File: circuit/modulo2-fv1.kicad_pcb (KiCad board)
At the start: 2 copper layers, 105 x 47 mm, 66 parts, among them J1 CONN_01X04, J2 POWER, J3 CONN_01X02, J4 HOLE, J5 HOLE, J6 USB_OTG, SW1 ROTENC_BOURNS_PEL12D, U1 NE5532, U10 TLE2426, U3 FV-1, U4 AVR-ISP6, U5 LM1117 3V3, U6 ATmega328p, U7 DBG_UART, U8 74164, Y1 16MHz

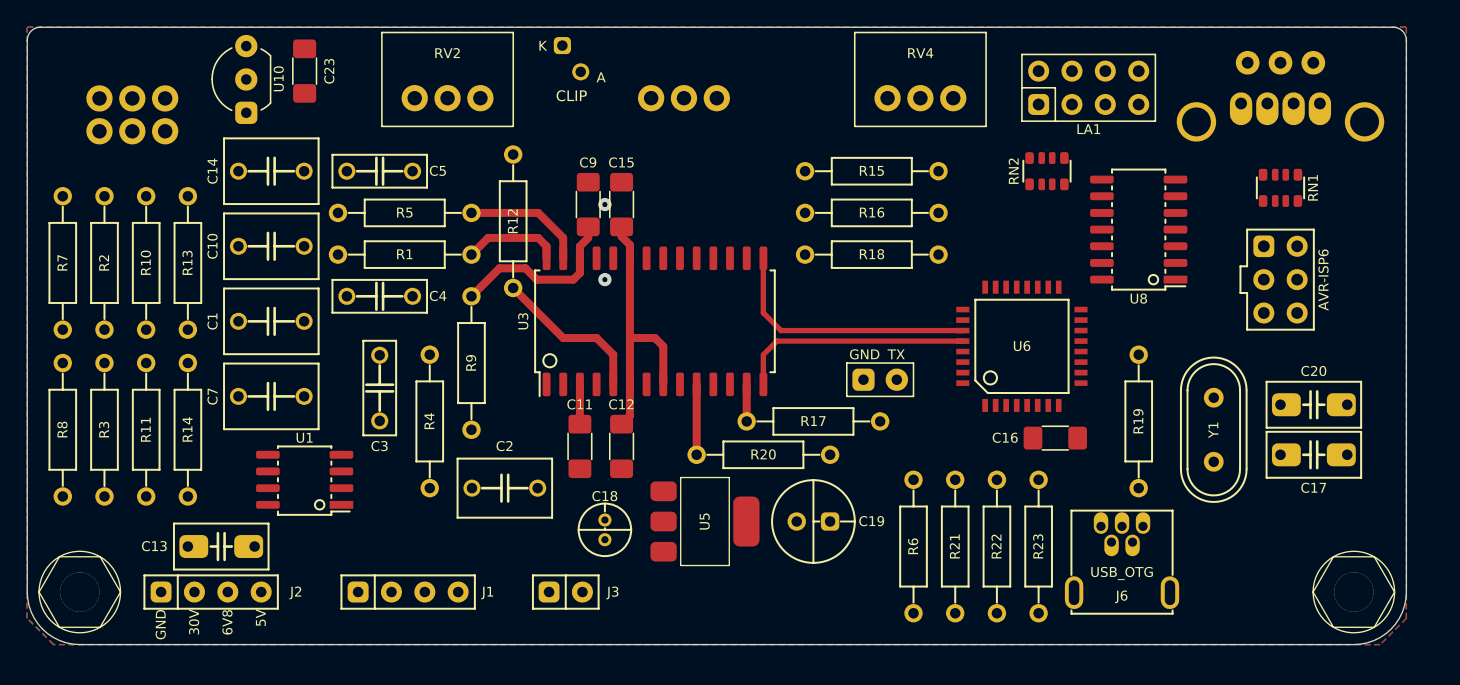
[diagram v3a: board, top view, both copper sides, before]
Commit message: routed pa27; routing fv-1
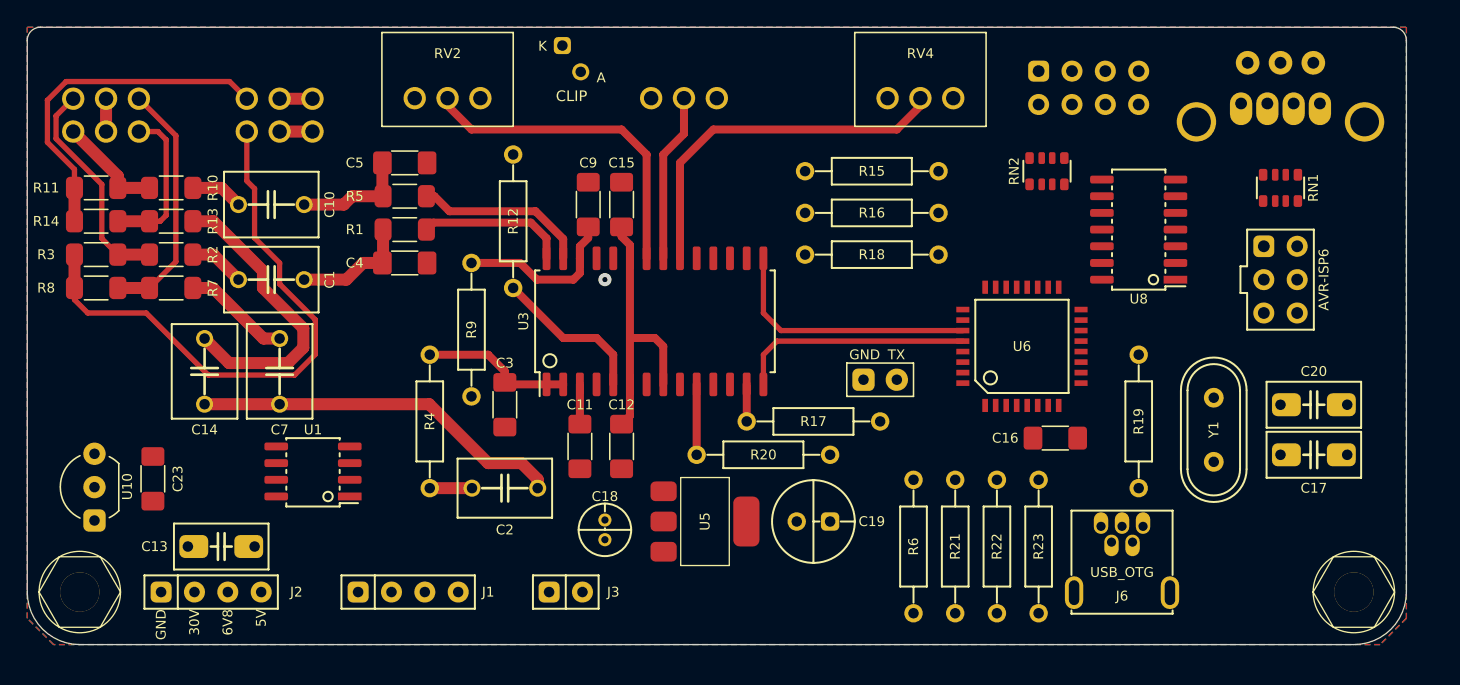
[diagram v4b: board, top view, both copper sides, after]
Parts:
- added RV5: A50K, myAmp:BOURNS_PTD902_xx15K, B.Cu at (69.2, 57.9)
- C3, C4, C5: footprint myAmp:C_FILM_L7.2mm_W2.5mm_P5.00mm -> myAmp:C_1206
- LA1: moved to B.Cu
- R1, R10, R11, R13, R14, R2, R3, R5, R7, R8: footprint myAmp:R_10MM -> myAmp:R_1206
- R23: value 1K5 -> 1M
- moved U10 33.1 mm to (55.1, 85.0)
- moved C23 33.1 mm to (59.6, 84.4)
- moved R11 18.8 mm to (55.2, 62.2), turned to 180 degrees
- moved R14 17.3 mm to (55.2, 64.8), turned to 180 degrees
- moved C14 16.1 mm to (63.5, 76.2), turned to 90 degrees
- moved R3 13.4 mm to (55.2, 67.3), turned to 180 degrees
- moved R8 11.1 mm to (55.2, 69.8), turned to 180 degrees
- moved C3 9.61 mm to (86.4, 78.7)
- moved R7 8.47 mm to (61.0, 69.8), turned to 180 degrees
- moved R10 6.02 mm to (61.0, 62.2), turned to 180 degrees
- moved R2 5.12 mm to (61.0, 67.3), turned to 180 degrees
- moved R13 3.42 mm to (61.0, 64.8), turned to 180 degrees
- moved C4 3.18 mm to (78.7, 67.9)
- moved C1 3.17 mm to (68.6, 69.2)
- moved C10 3.17 mm to (68.6, 63.5)
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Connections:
- R11 pad 2: Net-(R11-Pad2) -> Net-(RV5-Pad4)
- R14 pad 2: Net-(R11-Pad2) -> Net-(RV5-Pad4)
- R3 pad 2: Net-(R3-Pad2) -> Net-(RV5-Pad1)
- R8 pad 2: Net-(R3-Pad2) -> Net-(RV5-Pad1)
- RV1 pad 1: Net-(R2-Pad2) -> Net-(R10-Pad2)
- RV1 pad 3: Net-(R7-Pad2) -> Net-(R13-Pad2)
- RV1 pad 4: Net-(R10-Pad2) -> Net-(R2-Pad2)
- RV1 pad 6: Net-(R13-Pad2) -> Net-(R7-Pad2)
- U1 pad 2: /OUTL -> Net-(RV5-Pad1)
- U1 pad 3: Net-(R3-Pad2) -> VGND
- U1 pad 5: Net-(R11-Pad2) -> VGND
- U1 pad 6: /OUTR -> Net-(RV5-Pad4)
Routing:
- net Net-(RV5-Pad1): track 0.00 -> 43.9 mm
- net IN: track 0.00 -> 28.4 mm
- net Net-(RV4-Pad2): track 0.00 -> 28.0 mm
- net Net-(RV5-Pad4): track 0.00 -> 26.4 mm
- net Net-(RV2-Pad2): track 0.00 -> 25.2 mm
- net Net-(C14-Pad2): track 0.00 -> 22.8 mm
- net Net-(R7-Pad2): track 0.00 -> 18.8 mm
- net Net-(R2-Pad2): track 0.00 -> 16.8 mm
- net Net-(RV3-Pad2): track 0.00 -> 12.8 mm
- net Net-(R13-Pad2): track 0.00 -> 12.0 mm
- net Net-(C3-Pad2): track 0.00 -> 11.6 mm
- net /FVL: track 0.00 -> 9.05 mm
- net /FVR: track 0.00 -> 8.83 mm
- net Net-(C7-Pad2): track 0.00 -> 8.20 mm
- net Net-(R10-Pad2): track 0.00 -> 8.11 mm
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
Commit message: further routing of FV-1
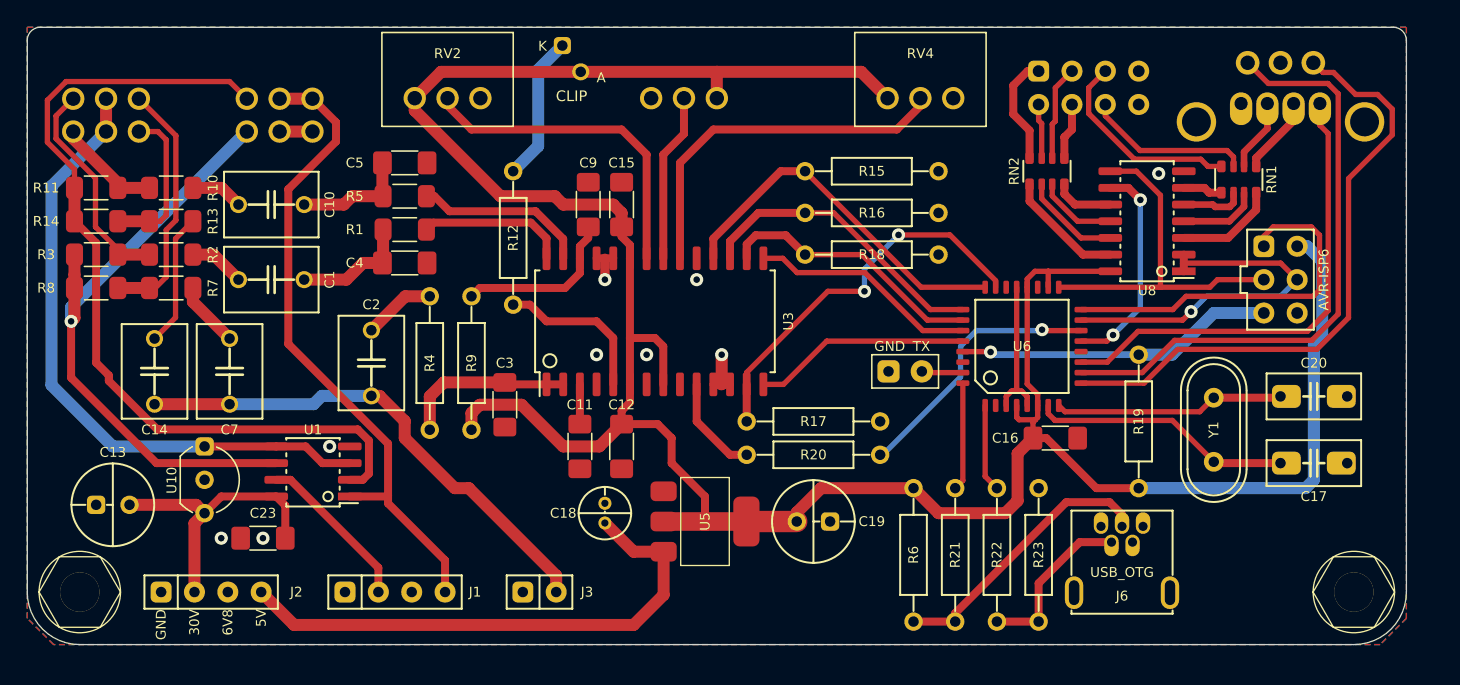
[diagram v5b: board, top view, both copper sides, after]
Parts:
- C13: value 100nF -> 10uF; footprint myAmp:C_5MM_1206 -> myAmp:CPOL_D6.3_P2.5
- C2: footprint myAmp:C_FILM_L7.2mm_W4.5mm_P5.00mm -> myAmp:C_FILM_L7.2mm_W5.0mm_P5.00mm
- moved C2 13.9 mm to (76.2, 75.6), turned to -90 degrees
- moved C23 9.52 mm to (67.9, 88.9), turned to 0 degrees
- moved C13 8.84 mm to (56.5, 86.4)
- moved U10 8.40 mm to (63.5, 84.5), turned to -90 degrees
- moved R4 4.45 mm to (80.6, 75.6), turned to -90 degrees
- moved C14 3.81 mm to (59.7, 76.2)
- moved C7 3.81 mm to (65.4, 76.2)
- moved R20 3.81 mm to (109.9, 82.5)
- moved RN1 3.24 mm to (142.2, 61.6)
- moved R9 2.54 mm to (83.8, 75.6)
- moved U7 2.01 mm to (116.8, 76.2)
- moved J3 2.00 mm to (89.0, 93.0)
- moved R12 1.27 mm to (87.0, 66.0)
- moved C18 1.27 mm to (94.0, 87.0)
- moved J1 1.00 mm to (78.0, 93.0)
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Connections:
- C13 pad 1: GND -> +24V
- C13 pad 2: +24V -> GND
- R11 pad 2: Net-(RV5-Pad4) -> Net-(R11-Pad2)
- R14 pad 2: Net-(RV5-Pad4) -> Net-(R11-Pad2)
- R3 pad 2: Net-(RV5-Pad1) -> Net-(R3-Pad2)
- R8 pad 2: Net-(RV5-Pad1) -> Net-(R3-Pad2)
- RV5 pad 1: Net-(RV5-Pad1) -> Net-(R3-Pad2)
- RV5 pad 4: Net-(RV5-Pad4) -> Net-(R11-Pad2)
- U1 pad 1: /OUTL -> /OUTR
- U1 pad 2: Net-(RV5-Pad1) -> Net-(R11-Pad2)
- U1 pad 6: Net-(RV5-Pad4) -> Net-(R3-Pad2)
- U1 pad 7: /OUTR -> /OUTL
- U6 pad 13: unconnected-(U6-Pad13) -> /LED_RST
- U6 pad 23: /LED_RST -> /T0
- U6 pad 30: /T0 -> unconnected-(U6-Pad30)
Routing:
- net +3V3: track 21.2 -> 208.7 mm
- net Net-(R11-Pad2): track 0.00 -> 65.5 mm
- net Net-(R3-Pad2): track 0.00 -> 47.8 mm, vias 0 -> 1
- net /OUTR: track 2.50 -> 50.2 mm
- net /ROT_B: track 0.00 -> 47.2 mm
- net VGND: track 2.50 -> 48.7 mm
- net /ROT_A: track 0.00 -> 46.1 mm
- net Net-(RV5-Pad1): track 43.9 -> 0.00 mm
- net +5V: track 0.00 -> 41.3 mm
- net /ROT_SW: track 0.00 -> 36.5 mm
- net /MISO: track 0.00 -> 28.5 mm
- net /MOSI: track 0.00 -> 28.2 mm, vias 0 -> 1
- net /S2: track 0.00 -> 28.0 mm
- net /SCK: track 0.00 -> 27.4 mm
- net /T0: track 2.82 -> 30.0 mm, vias 0 -> 2
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
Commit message: no more assembler; more routing
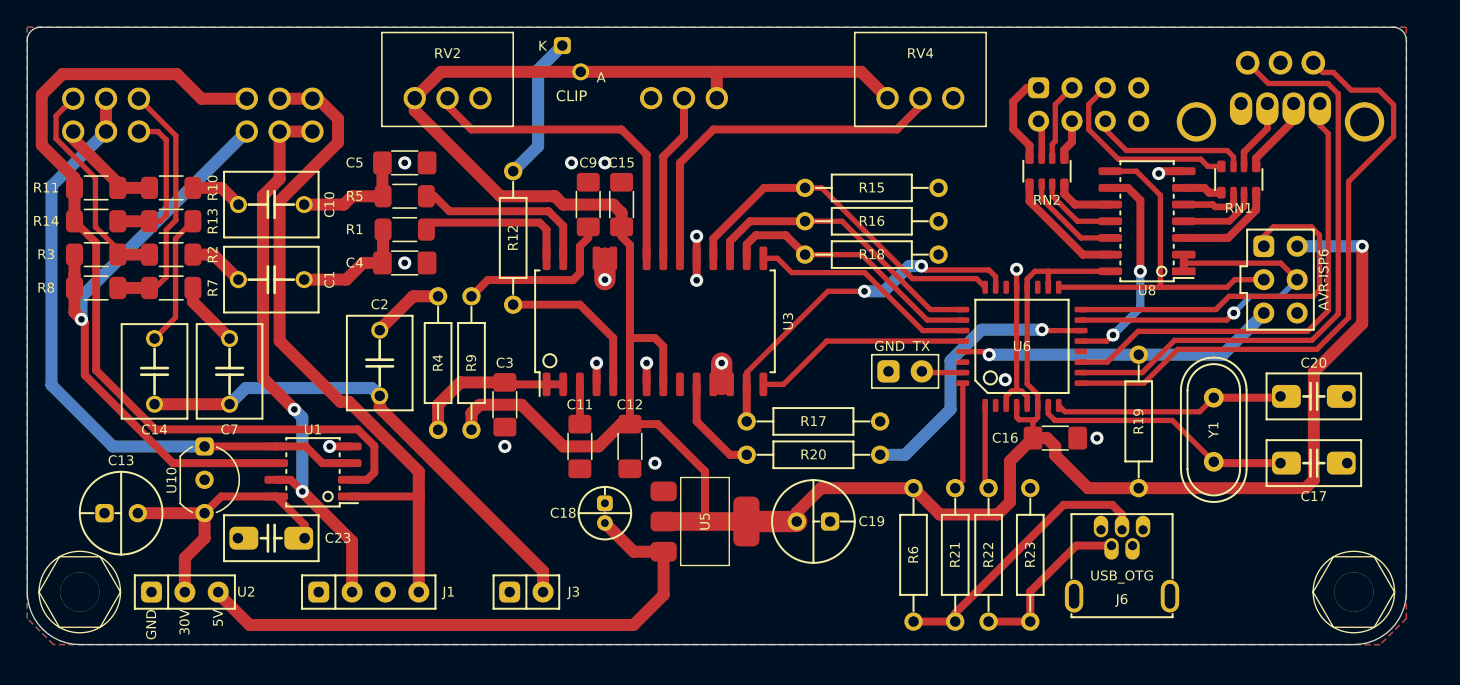
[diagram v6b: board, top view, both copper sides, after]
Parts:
- removed J2: POWER, myAmp:POWER
- added U2: POWER, myAmp:PWR_CONN, F.Cu at (62.0, 93.0)
- C23: footprint myAmp:C_1206 -> myAmp:C_5MM_1206
- moved J1 2.00 mm to (76.0, 93.0)
- moved LA1 1.27 mm to (130.8, 55.9)
- moved R15 1.27 mm to (114.3, 62.2)
- moved J3 1.00 mm to (88.0, 93.0)
- moved C13 0.90 mm to (57.1, 87.0)
- moved C12 0.64 mm to (95.9, 81.9)
- moved C23 0.64 mm to (68.6, 88.9)
- moved R22 0.64 mm to (123.2, 90.2)
- moved R23 0.64 mm to (126.4, 90.2)
- moved R4 0.64 mm to (81.3, 75.6)
- moved C2 0.63 mm to (76.8, 75.6)
- moved R16 0.63 mm to (114.3, 64.8)
- moved J6 0.27 mm to (133.3, 88.3)
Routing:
- net /OUTL: track 14.9 -> 43.3 mm, vias 0 -> 2
- net GND: track 17.7 -> 26.0 mm, vias 9 -> 17
- net +3V3: track 208.7 -> 213.6 mm, vias 0 -> 1
- net +5V: track 41.3 -> 44.6 mm
- net /OUTR: track 50.2 -> 53.0 mm
- net /T0: track 30.0 -> 27.2 mm
- net Net-(R11-Pad2): track 65.5 -> 67.4 mm
- net Net-(R3-Pad2): track 47.8 -> 46.4 mm
- net Net-(LA1-Pad3): track 7.24 -> 5.97 mm
- net Net-(LA1-Pad4): track 4.32 -> 3.05 mm
- net Net-(LA1-Pad2): track 4.18 -> 2.91 mm
- net Net-(LA1-Pad1): track 8.42 -> 7.18 mm
- net /S2: track 28.0 -> 26.9 mm
- net Net-(C3-Pad2): track 13.2 -> 12.2 mm
- net /FV_CLK: track 20.6 -> 21.4 mm
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
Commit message: getting closer to the final PCBs; still have to change the rotenc
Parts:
- added C6: 1nF, myAmp:C_1206, F.Cu at (124.5, 65.4)
- added R24: 10K, myAmp:R_10MM, F.Cu at (74.3, 78.7)
- added R25: 1K, myAmp:R_10MM, F.Cu at (74.3, 74.9)
- added U9: AMPCTRL, myAmp:PIN_1x03, F.Cu at (95.0, 93.0)
- U2: value POWER -> PWR_CONN
- moved R9 18.1 mm to (89.5, 58.4), turned to -90 degrees
- moved R4 6.54 mm to (87.0, 78.7)
- moved C2 6.48 mm to (83.2, 76.8)
- moved C3 4.49 mm to (89.5, 81.9)
- moved J3 3.00 mm to (85.0, 93.0)
- moved J1 2.00 mm to (74.0, 93.0)
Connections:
- U6 pad 2: unconnected-(U6-Pad2) -> /POW_MUTE
- U6 pad 22: unconnected-(U6-Pad22) -> /IN_V
- U6 pad 30: unconnected-(U6-Pad30) -> /POW_RST
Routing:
- net /IN_V: track 0.00 -> 57.6 mm, vias 0 -> 4
- net /POW_RST: track 0.00 -> 43.1 mm, vias 0 -> 2
- net /POW_MUTE: track 0.00 -> 42.6 mm, vias 0 -> 2
- net +3V3: track 213.6 -> 197.0 mm
- net +24V: track 21.8 -> 32.7 mm
- net /REFP: track 12.8 -> 6.53 mm
- net +5V: track 44.6 -> 40.9 mm
- net /OUTR: track 53.0 -> 49.4 mm
- net Net-(C3-Pad2): track 12.2 -> 8.95 mm
- net IN: track 38.0 -> 40.2 mm
- net Net-(C2-Pad1): track 5.54 -> 4.09 mm
- net GND: track 26.0 -> 24.7 mm, vias 17 -> 16
- net Net-(R1-Pad2): track 11.8 -> 10.5 mm
- net Net-(D1-Pad1): track 11.1 -> 12.2 mm
- net Net-(R5-Pad2): track 13.8 -> 13.0 mm
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
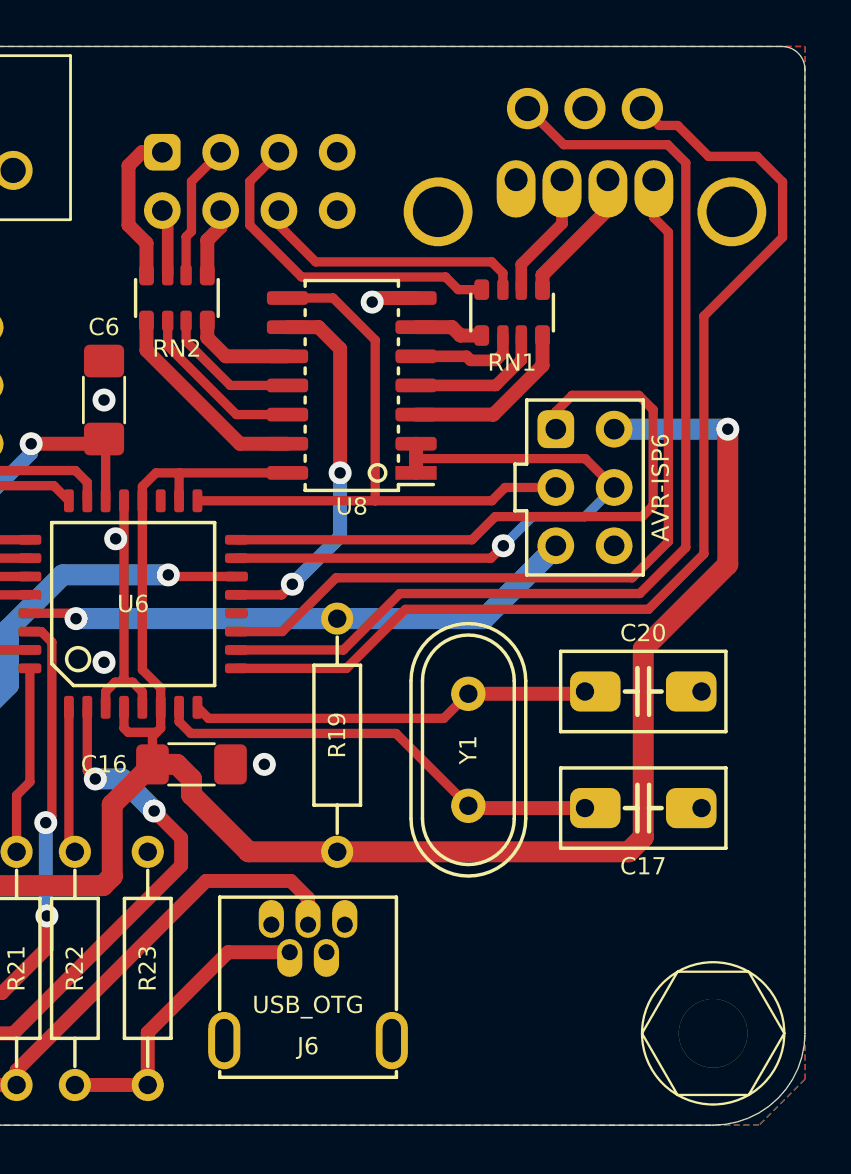
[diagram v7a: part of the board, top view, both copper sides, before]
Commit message: usb has been changed to accommodate fab capabilities; moved the rotenc deeper into the board
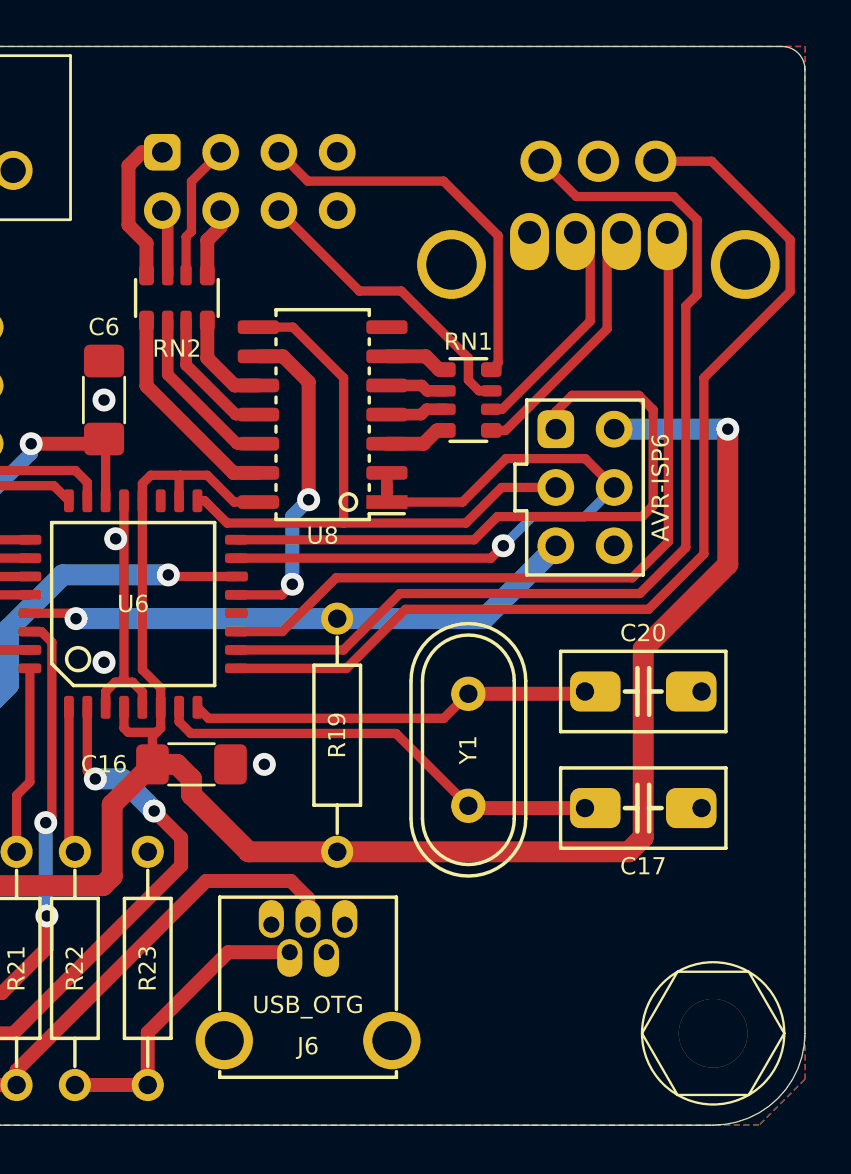
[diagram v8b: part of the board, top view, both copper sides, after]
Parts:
- J6: footprint myAmp:USB_OTG_THT -> myAmp:USB_OTG_THT_simple
- moved RN1 4.26 mm to (140.3, 65.4), turned to -90 degrees
- moved SW1 2.37 mm to (146.0, 55.0)
- moved U8 1.80 mm to (134.0, 66.0)
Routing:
- net GR_ROTENC: track 5.97 -> 11.3 mm
- net Net-(RN1-Pad4): track 7.70 -> 2.79 mm
- net BL_ROTENC: track 5.53 -> 10.0 mm
- net Net-(RN1-Pad3): track 6.11 -> 2.65 mm
- net /ROT_B: track 47.5 -> 45.0 mm
- net /ROT_SW: track 36.5 -> 34.2 mm
- net /ROT_A: track 46.1 -> 43.8 mm
- net Net-(RN1-Pad2): track 4.77 -> 2.65 mm
- net /MOSI: track 28.2 -> 30.2 mm
- net Net-(LA1-Pad5): track 15.0 -> 17.0 mm
- net /LED_RST: track 16.4 -> 14.4 mm
- net GND: track 24.7 -> 22.7 mm, vias 16 -> 15
- net Net-(LA1-Pad6): track 12.0 -> 13.1 mm
- net +3V3: track 197.0 -> 196.1 mm
